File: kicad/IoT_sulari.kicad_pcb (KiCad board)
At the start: 2 copper layers, 5 parts, among them U1 HDC2010YPAR, U2 NRF9160-SICA-B1A-R, U3 TMP117MAIDRVT, U4 TPD3F303DPVR, U5 TCR2EF33

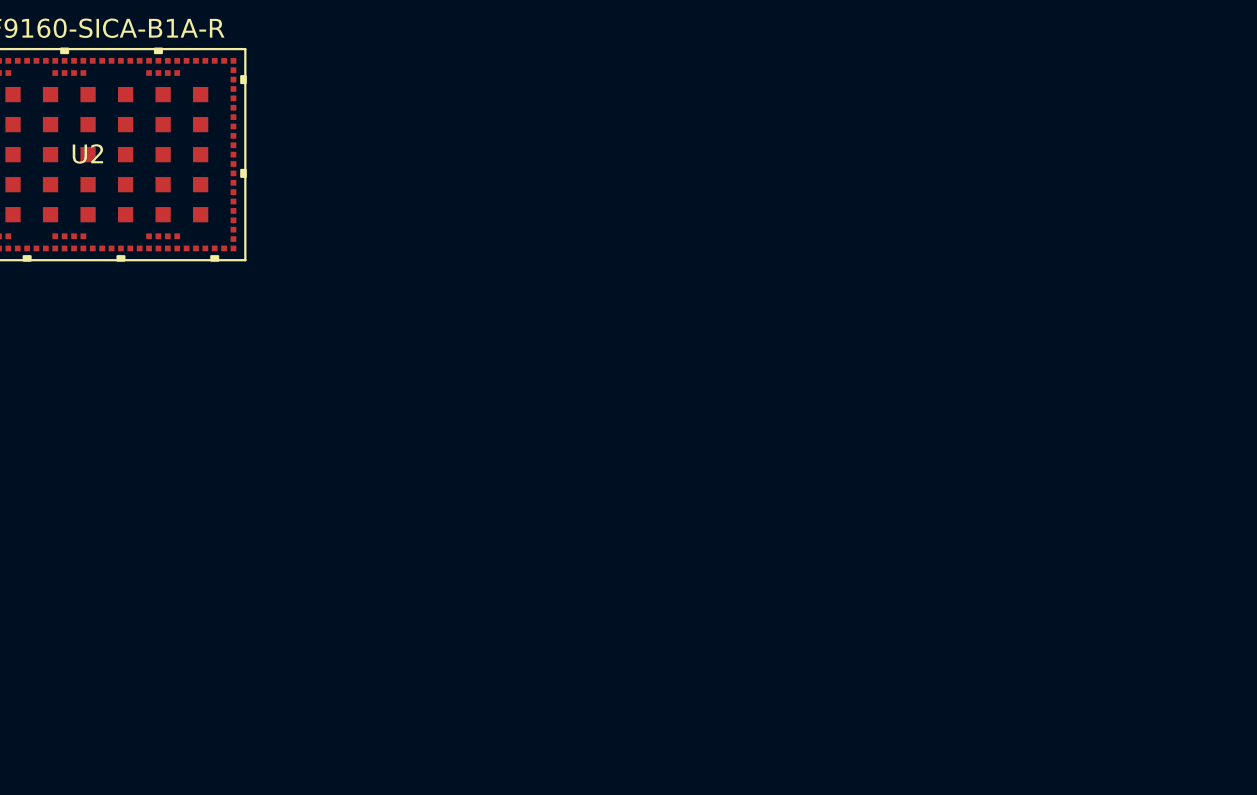
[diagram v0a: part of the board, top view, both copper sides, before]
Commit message: Added Digikey part number and footprint to symbols, added signal TMP_ALERT
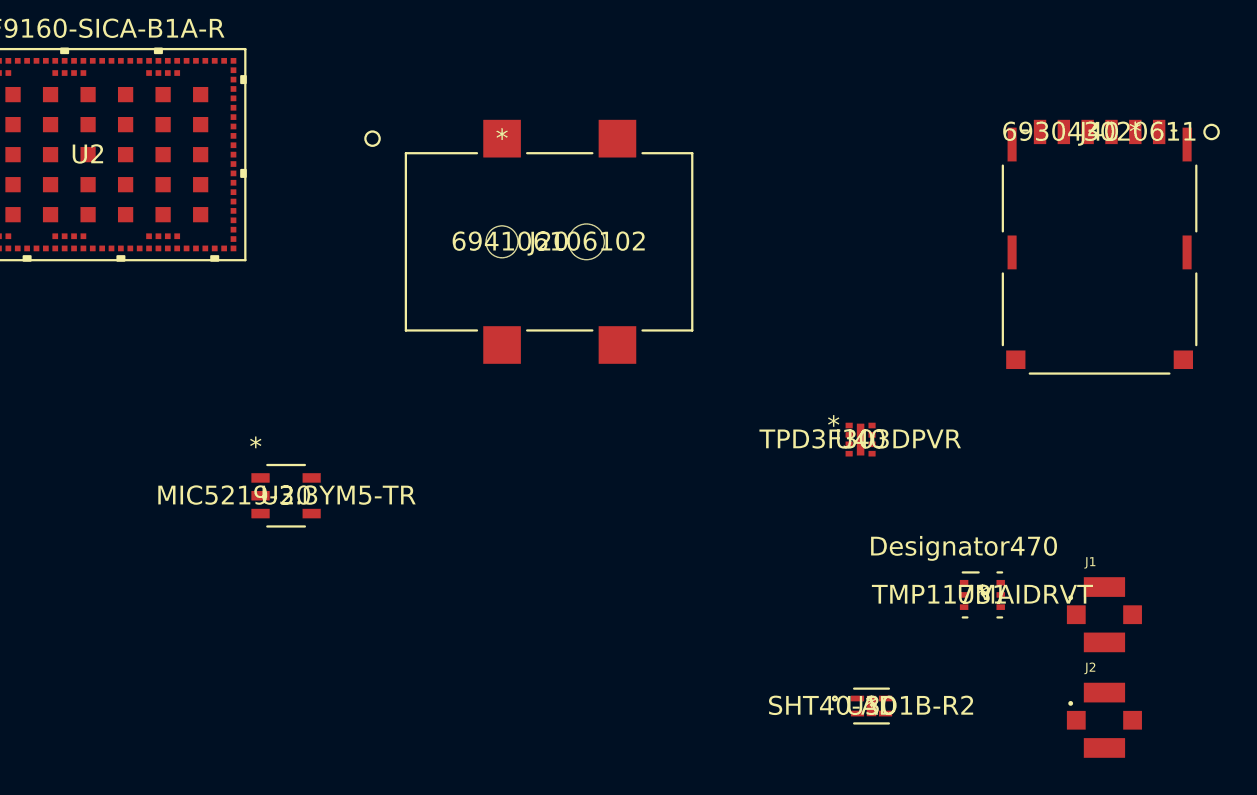
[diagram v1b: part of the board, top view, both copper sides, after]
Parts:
- added J1: 73412-0110, 73412-0110:MOLEX_73412-0110, F.Cu at (155.3, 84.2)
- added J2: 73412-0110, 73412-0110:MOLEX_73412-0110, F.Cu at (155.3, 89.9)
- added J20: 694106106102, 694106106102:694106106102, F.Cu at (123.2, 58.9)
- added J40: 693043020611, 693043020611:693043020611, F.Cu at (156.9, 58.5)
- added U20: MIC5219-3.3YM5-TR, MIC5219-3.3YM5-TR:MIC5219-3.3YM5-TR, F.Cu at (111.7, 77.9)
- added U30: SHT40-AD1B-R2, SHT-40AD1B-R2:SHT40-AD1B-R2, F.Cu at (142.9, 89.1)
- added U31: TMP117MAIDRVT, TMP117MAIDRVT:TMP117MAIDRVT, F.Cu at (148.8, 83.2)
- added U40: TPD3F303DPVR, TPD3F303DPVR:TPD3F303DPVR, F.Cu at (142.3, 74.9)
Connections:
- U2 pad 1: unconnected-(U2A-GND_SHIELD-Pad1) -> GND
- U2 pad 100: (no net) -> unconnected-(U2A-P0-04-Pad100)
- U2 pad 101: (no net) -> Net-(U2A-ENABLE)
- U2 pad 102: (no net) -> Net-(U2A-VDD1)
- U2 pad 103: (no net) -> GND
- U2 pad 104: (no net) -> unconnected-(U2B-RESERVED-Pad104)
- U2 pad 105: (no net) -> unconnected-(U2B-RESERVED-Pad105)
- U2 pad 106: (no net) -> unconnected-(U2B-RESERVED-Pad106)
- U2 pad 107: (no net) -> unconnected-(U2B-RESERVED-Pad107)
- U2 pad 108: (no net) -> unconnected-(U2B-RESERVED-Pad108)
- U2 pad 109: (no net) -> unconnected-(U2B-RESERVED-Pad109)
- U2 pad 11: unconnected-(U2A-GND_SHIELD-Pad11) -> GND
- U2 pad 110: (no net) -> unconnected-(U2B-RESERVED-Pad110)
- U2 pad 111: (no net) -> unconnected-(U2B-RESERVED-Pad111)
- U2 pad 112: (no net) -> unconnected-(U2B-RESERVED-Pad112)
- U2 pad 113: (no net) -> unconnected-(U2B-RESERVED-Pad113)
- U2 pad 114: (no net) -> unconnected-(U2B-RESERVED-Pad114)
- U2 pad 115: (no net) -> unconnected-(U2B-RESERVED-Pad115)
- U2 pad 116: (no net) -> unconnected-(U2B-RESERVED-Pad116)
- U2 pad 117: (no net) -> unconnected-(U2B-RESERVED-Pad117)
- U2 pad 118: (no net) -> unconnected-(U2B-RESERVED-Pad118)
- U2 pad 119: (no net) -> unconnected-(U2B-RESERVED-Pad119)
- U2 pad 12: unconnected-(U2A-VDD_GPIO-Pad12) -> +3.3V
- U2 pad 120: (no net) -> unconnected-(U2B-RESERVED-Pad120)
- U2 pad 121: (no net) -> unconnected-(U2B-RESERVED-Pad121)
- U2 pad 122: (no net) -> unconnected-(U2B-RESERVED-Pad122)
- U2 pad 123: (no net) -> unconnected-(U2B-RESERVED-Pad123)
- U2 pad 124: (no net) -> unconnected-(U2B-RESERVED-Pad124)
- U2 pad 125: (no net) -> unconnected-(U2B-RESERVED-Pad125)
- U2 pad 126: (no net) -> unconnected-(U2B-RESERVED-Pad126)
- U2 pad 127: (no net) -> unconnected-(U2B-RESERVED-Pad127)
- U2 pad 13: unconnected-(U2A-DEC0-Pad13) -> Net-(U2A-DEC0)
- U2 pad 14: unconnected-(U2A-GND_SHIELD-Pad14) -> GND
- U2 pad 17: unconnected-(U2A-GND_SHIELD-Pad17) -> GND
- U2 pad 21: unconnected-(U2A-GND_SHIELD-Pad21) -> GND
- U2 pad 22: unconnected-(U2A-VDD2-Pad22) -> +3.3V
- U2 pad 27: unconnected-(U2A-GND_SHIELD-Pad27) -> GND
- U2 pad 31: unconnected-(U2A-GND_SHIELD-Pad31) -> GND
- U2 pad 32: unconnected-(U2A-NRESET-Pad32) -> Net-(U2A-NRESET)
- U2 pad 36: unconnected-(U2A-GND_SHIELD-Pad36) -> GND
- U2 pad 41: unconnected-(U2A-GND_SHIELD-Pad41) -> GND
- U2 pad 43: unconnected-(U2A-SIM_RST-Pad43) -> SIM_RST
- U2 pad 44: unconnected-(U2A-GND_SHIELD-Pad44) -> GND
- U2 pad 46: unconnected-(U2A-SIM_CLK-Pad46) -> SIM_CLK
- U2 pad 47: unconnected-(U2A-GND_SHIELD-Pad47) -> GND
- U2 pad 48: unconnected-(U2A-SM_IO-Pad48) -> SIM_IO
- U2 pad 49: unconnected-(U2A-SIM_1V8-Pad49) -> SIM_1V8
- U2 pad 5: unconnected-(U2A-GND_SHIELD-Pad5) -> GND
- U2 pad 50: unconnected-(U2A-GND_SHIELD-Pad50) -> GND
- U2 pad 52: unconnected-(U2A-GND_SHIELD-Pad52) -> GND
- U2 pad 56: unconnected-(U2A-GND_SHIELD-Pad56) -> GND
- U2 pad 6: unconnected-(U2A-GND_SHIELD-Pad6) -> GND
- U2 pad 60: unconnected-(U2A-GND_SHIELD-Pad60) -> GND
- U2 pad 61: unconnected-(U2A-ANT-Pad61) -> Net-(J2-SIG)
- U2 pad 62: unconnected-(U2A-GND_SHIELD-Pad62) -> GND
- U2 pad 63: unconnected-(U2A-GND_SHIELD-Pad63) -> GND
- U2 pad 65: unconnected-(U2A-GND_SHIELD-Pad65) -> GND
- U2 pad 66: unconnected-(U2A-GND_SHIELD-Pad66) -> GND
- U2 pad 67: unconnected-(U2A-GPS-Pad67) -> Net-(J1-SIG)
- U2 pad 68: unconnected-(U2A-GND_SHIELD-Pad68) -> GND
- U2 pad 69: unconnected-(U2A-GND_SHIELD-Pad69) -> GND
- U2 pad 7: unconnected-(U2A-GND_SHIELD-Pad7) -> GND
- U2 pad 72: unconnected-(U2A-GND_SHIELD-Pad72) -> GND
- U2 pad 74: unconnected-(U2A-GND_SHIELD-Pad74) -> GND
- U2 pad 75: unconnected-(U2A-GND_SHIELD-Pad75) -> GND
- U2 pad 76: unconnected-(U2A-GND_SHIELD-Pad76) -> GND
- U2 pad 77: unconnected-(U2A-GND_SHIELD-Pad77) -> GND
- U2 pad 78: unconnected-(U2A-GND_SHIELD-Pad78) -> GND
- U2 pad 79: unconnected-(U2A-GND_SHIELD-Pad79) -> GND
- U2 pad 8: unconnected-(U2A-GND_SHIELD-Pad8) -> GND
- U2 pad 80: unconnected-(U2A-GND_SHIELD-Pad80) -> GND
- U2 pad 81: unconnected-(U2A-GND_SHIELD-Pad81) -> GND
- U2 pad 82: (no net) -> GND
- U2 pad 83: (no net) -> I2C/SDA
- U2 pad 84: (no net) -> I2C/SCL
- U2 pad 85: (no net) -> GND
- U2 pad 86: (no net) -> TMP_ALERT
- U2 pad 87: (no net) -> unconnected-(U2A-P0-29-Pad87)
- U2 pad 88: (no net) -> unconnected-(U2A-P0-30-Pad88)
- U2 pad 89: (no net) -> unconnected-(U2A-P0-31-Pad89)
- U2 pad 9: unconnected-(U2A-GND_SHIELD-Pad9) -> GND
- U2 pad 90: (no net) -> GND
- U2 pad 91: (no net) -> unconnected-(U2A-COEX2-Pad91)
- U2 pad 92: (no net) -> unconnected-(U2A-COEX1-Pad92)
- U2 pad 93: (no net) -> unconnected-(U2A-COEX0-Pad93)
- U2 pad 94: (no net) -> GND
- U2 pad 95: (no net) -> STATUS_LED_RED
- U2 pad 96: (no net) -> STATUS_LED_GREEN
- U2 pad 97: (no net) -> unconnected-(U2A-P0-02-Pad97)
- U2 pad 98: (no net) -> GND
- U2 pad 99: (no net) -> unconnected-(U2A-P0-03-Pad99)

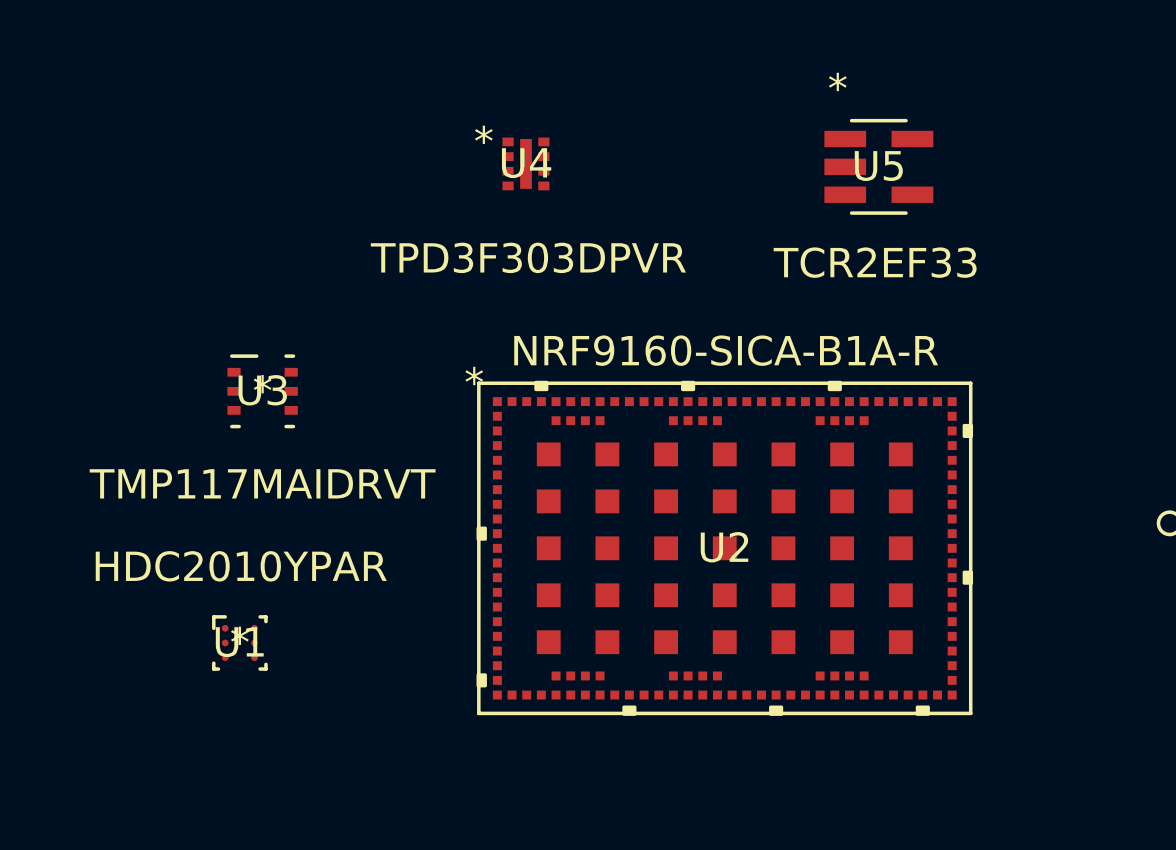
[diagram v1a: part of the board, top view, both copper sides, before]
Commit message: schematic editing, led selection
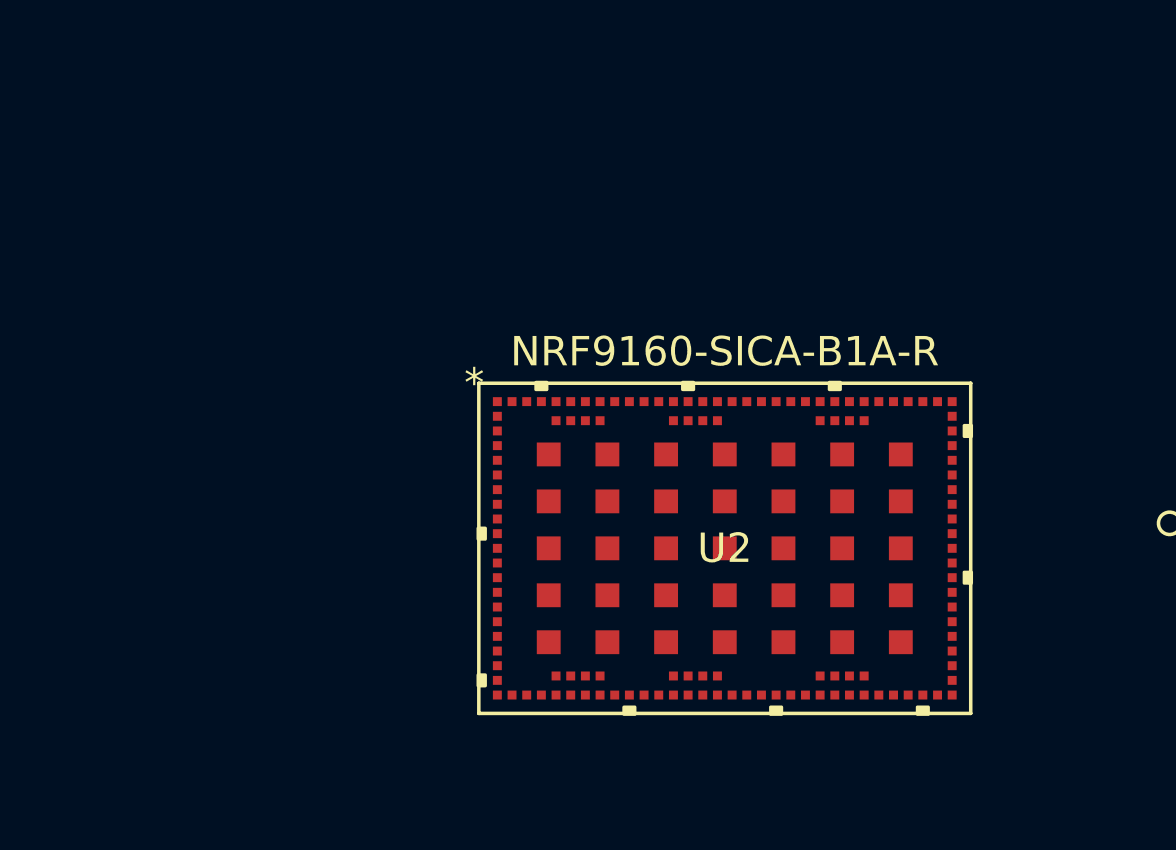
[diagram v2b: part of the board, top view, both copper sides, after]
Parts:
- removed U1: HDC2010YPAR, HDC2010YPAR:HDC2020YPAR
- removed U3: TMP117MAIDRVT, TMP117MAIDRVT:TMP117MAIDRVT
- removed U4: TPD3F303DPVR, TPD3F303DPVR:TPD3F303DPVR
- removed U5: TCR2EF33, TCR2EF33:TCR2EF33

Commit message: PCB update
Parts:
- added C1: 15p, Capacitor_SMD:C_0603_1608Metric_Pad1.08x0.95mm_HandSolder, F.Cu at (88.1, 102.9)
- added C10: 100n, Capacitor_SMD:C_0603_1608Metric_Pad1.08x0.95mm_HandSolder, F.Cu at (92.5, 113.0)
- added C2: 100n, Capacitor_SMD:C_0603_1608Metric_Pad1.08x0.95mm_HandSolder, F.Cu at (88.1, 105.4)
- added C20: 100n, Capacitor_SMD:C_0603_1608Metric_Pad1.08x0.95mm_HandSolder, F.Cu at (114.8, 108.9)
- added C21: 2.2u, Capacitor_SMD:C_0603_1608Metric_Pad1.08x0.95mm_HandSolder, F.Cu at (114.6, 113.0)
- added C22: 470p, Capacitor_SMD:C_0603_1608Metric_Pad1.08x0.95mm_HandSolder, F.Cu at (114.6, 117.4)
- added C3: 47u, Capacitor_SMD:C_0603_1608Metric_Pad1.08x0.95mm_HandSolder, F.Cu at (88.1, 108.0)
- added C30: 100n, Capacitor_SMD:C_0603_1608Metric_Pad1.08x0.95mm_HandSolder, F.Cu at (196.9, 100.6)
- added C31: 100n, Capacitor_SMD:C_0603_1608Metric_Pad1.08x0.95mm_HandSolder, F.Cu at (196.9, 103.1)
- added C4: 15p, Capacitor_SMD:C_0603_1608Metric_Pad1.08x0.95mm_HandSolder, F.Cu at (88.1, 110.5)
- added C5: 100n, Capacitor_SMD:C_0603_1608Metric_Pad1.08x0.95mm_HandSolder, F.Cu at (88.1, 113.0)
- added C6: 47u, Capacitor_SMD:C_0603_1608Metric_Pad1.08x0.95mm_HandSolder, F.Cu at (92.5, 102.9)
- added C7: 100n, Capacitor_SMD:C_0603_1608Metric_Pad1.08x0.95mm_HandSolder, F.Cu at (92.5, 105.4)
- added C8: 4.7u, Capacitor_SMD:C_0603_1608Metric_Pad1.08x0.95mm_HandSolder, F.Cu at (92.5, 108.0)
- added C9: 4.7u, Capacitor_SMD:C_0603_1608Metric_Pad1.08x0.95mm_HandSolder, F.Cu at (92.5, 110.5)
- added D1: RED, LED_SMD:LED_0603_1608Metric_Pad1.05x0.95mm_HandSolder, F.Cu at (88.2, 115.5)
- added D2: GREEN, LED_SMD:LED_0603_1608Metric_Pad1.05x0.95mm_HandSolder, F.Cu at (88.2, 118.1)
- added FB1: 120R/0.70A, Resistor_SMD:R_0402_1005Metric_Pad0.72x0.64mm_HandSolder, F.Cu at (92.0, 115.2)
- added J7: ~, G800MJ302018EU:G800MJ302018EU, F.Cu at (121.1, 91.5)
- added R1: 10k, Resistor_SMD:R_0603_1608Metric_Pad0.98x0.95mm_HandSolder, F.Cu at (96.8, 102.9)
- added R2: 1k, Resistor_SMD:R_0603_1608Metric_Pad0.98x0.95mm_HandSolder, F.Cu at (96.8, 105.4)
- added R3: 7k, Resistor_SMD:R_0603_1608Metric_Pad0.98x0.95mm_HandSolder, F.Cu at (96.8, 108.0)
- added R30: 5k, Resistor_SMD:R_0603_1608Metric_Pad0.98x0.95mm_HandSolder, F.Cu at (196.9, 105.7)
- added R31: 5k, Resistor_SMD:R_0603_1608Metric_Pad0.98x0.95mm_HandSolder, F.Cu at (196.9, 108.2)
- added R32: 5k, Resistor_SMD:R_0603_1608Metric_Pad0.98x0.95mm_HandSolder, F.Cu at (196.9, 110.7)
- added R4: 7k, Resistor_SMD:R_0603_1608Metric_Pad0.98x0.95mm_HandSolder, F.Cu at (96.8, 110.5)
- added SW2: TL3301DF160QG, TL3301DF160QG:TL3301DF160QG, F.Cu at (79.5, 102.4)
- added SW3: TL3301DF160QG, TL3301DF160QG:TL3301DF160QG, F.Cu at (79.5, 116.0)
- added SW4: TL3301DF160QG, TL3301DF160QG:TL3301DF160QG, F.Cu at (79.5, 129.6)
- added SW5: TL3301DF160QG, TL3301DF160QG:TL3301DF160QG, F.Cu at (79.5, 143.1)
- moved U30 68.3 mm to (207.6, 111.0)
- moved U31 62.4 mm to (208.4, 101.7)
- moved J20 45.0 mm to (81.5, 41.7)
- moved J1 39.2 mm to (153.2, 45.1)
- moved J2 38.1 mm to (153.1, 51.9)
- moved U20 34.1 mm to (102.1, 45.1)
- moved U2 27.7 mm to (126.8, 49.2)
- moved J40 18.3 mm to (157.1, 76.8)
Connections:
- net USB_VBUS renamed Net-(U20-EN)
- J20 pad 3: USB_GND -> GND
- U2 pad 1: GND -> Net-(U2B-GND_SHIELD-Pad1)
- U2 pad 100: unconnected-(U2A-P0-04-Pad100) -> BUTTON3
- U2 pad 11: GND -> Net-(U2B-GND_SHIELD-Pad1)
- U2 pad 12: +3.3V -> Net-(U2A-VDD_GPIO)
- U2 pad 14: GND -> Net-(U2B-GND_SHIELD-Pad1)
- U2 pad 15: unconnected-(U2A-P0-08-Pad15) -> CLK
- U2 pad 16: unconnected-(U2A-P0-09-Pad16) -> CS
- U2 pad 17: GND -> Net-(U2B-GND_SHIELD-Pad1)
- U2 pad 18: unconnected-(U2A-P0-10-Pad18) -> DC
- U2 pad 19: unconnected-(U2A-P0-11-Pad19) -> RST
- U2 pad 2: unconnected-(U2A-P0-05-Pad2) -> BUTTON4
- U2 pad 20: unconnected-(U2A-P0-12-Pad20) -> BUSY
- U2 pad 21: GND -> Net-(U2B-GND_SHIELD-Pad1)
- U2 pad 22: +3.3V -> Net-(U2A-VDD2)
- U2 pad 23: unconnected-(U2A-P0-13/AIN0-Pad23) -> UART_RTS
- U2 pad 24: unconnected-(U2A-P0-14/AIN1-Pad24) -> UART_RXD
- U2 pad 25: unconnected-(U2A-P0-15/AIN2-Pad25) -> UART_TXD
- U2 pad 26: unconnected-(U2A-P0-16/AIN3-Pad26) -> UART_CTS
- U2 pad 27: GND -> Net-(U2B-GND_SHIELD-Pad1)
- U2 pad 31: GND -> Net-(U2B-GND_SHIELD-Pad1)
- U2 pad 33: unconnected-(U2A-SWDCLK-Pad33) -> SWDCLK
- U2 pad 34: unconnected-(U2A-SWDIO-Pad34) -> SWDIO
- U2 pad 36: GND -> Net-(U2B-GND_SHIELD-Pad1)
- U2 pad 4: unconnected-(U2A-P0-07-Pad4) -> DIN
- U2 pad 41: GND -> Net-(U2B-GND_SHIELD-Pad1)
- U2 pad 44: GND -> Net-(U2B-GND_SHIELD-Pad1)
- U2 pad 47: GND -> Net-(U2B-GND_SHIELD-Pad1)
- U2 pad 5: GND -> Net-(U2B-GND_SHIELD-Pad1)
- U2 pad 50: GND -> Net-(U2B-GND_SHIELD-Pad1)
- U2 pad 52: GND -> Net-(U2B-GND_SHIELD-Pad1)
- U2 pad 56: GND -> Net-(U2B-GND_SHIELD-Pad1)
- U2 pad 6: GND -> Net-(U2B-GND_SHIELD-Pad1)
- U2 pad 60: GND -> Net-(U2B-GND_SHIELD-Pad1)
- U2 pad 62: GND -> Net-(U2B-GND_SHIELD-Pad1)
- U2 pad 63: GND -> Net-(U2B-GND_SHIELD-Pad1)
- U2 pad 65: GND -> Net-(U2B-GND_SHIELD-Pad1)
- U2 pad 66: GND -> Net-(U2B-GND_SHIELD-Pad1)
- U2 pad 68: GND -> Net-(U2B-GND_SHIELD-Pad1)
- U2 pad 69: GND -> Net-(U2B-GND_SHIELD-Pad1)
- U2 pad 7: GND -> Net-(U2B-GND_SHIELD-Pad1)
- U2 pad 72: GND -> Net-(U2B-GND_SHIELD-Pad1)
- U2 pad 74: GND -> Net-(U2B-GND_SHIELD-Pad1)
- U2 pad 75: GND -> Net-(U2B-GND_SHIELD-Pad1)
- U2 pad 76: GND -> Net-(U2B-GND_SHIELD-Pad1)
- U2 pad 77: GND -> Net-(U2B-GND_SHIELD-Pad1)
- U2 pad 78: GND -> Net-(U2B-GND_SHIELD-Pad1)
- U2 pad 79: GND -> Net-(U2B-GND_SHIELD-Pad1)
- U2 pad 8: GND -> Net-(U2B-GND_SHIELD-Pad1)
- U2 pad 80: GND -> Net-(U2B-GND_SHIELD-Pad1)
- U2 pad 81: GND -> Net-(U2B-GND_SHIELD-Pad1)
- U2 pad 82: GND -> Net-(U2B-GND_SHIELD-Pad1)
- U2 pad 83: I2C/SDA -> SDA
- U2 pad 84: I2C/SCL -> SCL
- U2 pad 85: GND -> Net-(U2B-GND_SHIELD-Pad1)
- U2 pad 9: GND -> Net-(U2B-GND_SHIELD-Pad1)
- U2 pad 90: GND -> Net-(U2B-GND_SHIELD-Pad1)
- U2 pad 94: GND -> Net-(U2B-GND_SHIELD-Pad1)
- U2 pad 97: unconnected-(U2A-P0-02-Pad97) -> BUTTON1
- U2 pad 98: GND -> Net-(U2B-GND_SHIELD-Pad1)
- U2 pad 99: unconnected-(U2A-P0-03-Pad99) -> BUTTON2
- U30 pad 1: I2C/SDA -> /sensorboard/SDA
- U30 pad 2: I2C/SCL -> /sensorboard/SCL
- U30 pad 3: +3.3V -> /sensorboard/VCC
- U30 pad 4: GND -> /sensorboard/GND
- U31 pad 1: I2C/SCL -> /sensorboard/SCL
- U31 pad 2: GND -> /sensorboard/GND
- U31 pad 3: TMP_ALERT -> /sensorboard/TMP_ALERT
- U31 pad 4: +3.3V -> /sensorboard/VCC
- U31 pad 5: +3.3V -> /sensorboard/VCC
- U31 pad 6: I2C/SDA -> /sensorboard/SDA
